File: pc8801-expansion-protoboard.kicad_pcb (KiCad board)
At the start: 2 copper layers, 219 x 95 mm, 13 parts, among them J1 Solder Side, J2 Parts Side, J3 5V, J4 12V, J5 -12V, J6 GND_1, J7 GND_2, U1 ExpansionEdge

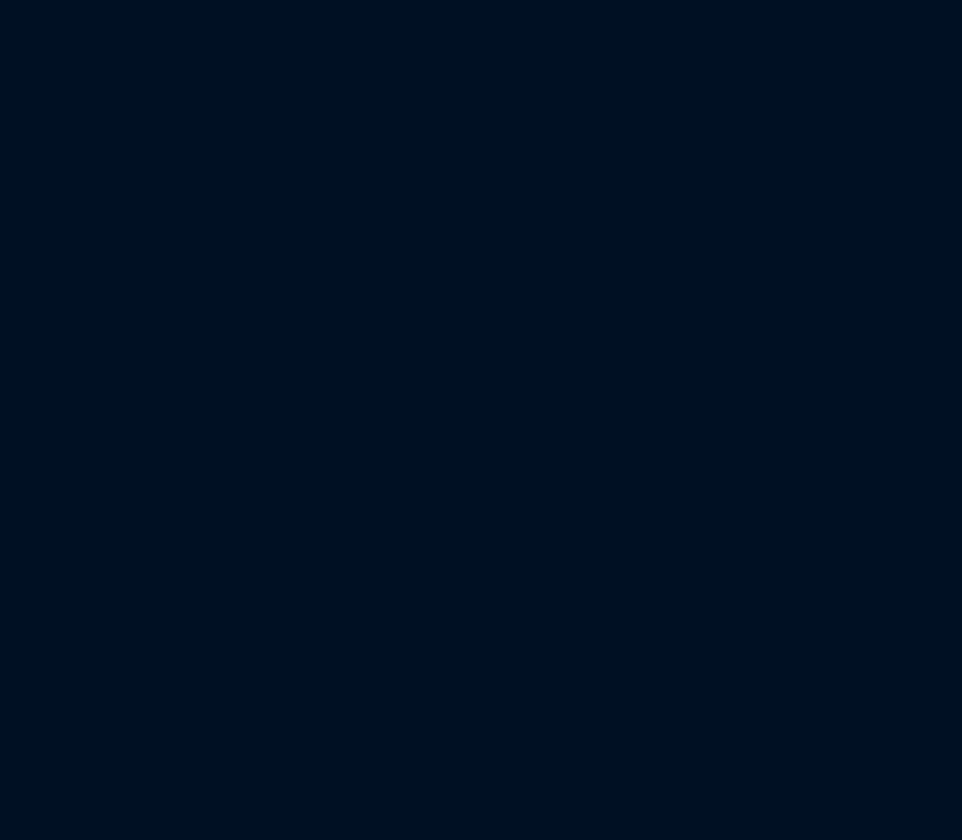
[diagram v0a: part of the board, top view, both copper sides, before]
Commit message: Flip-flops and SPI clocks added
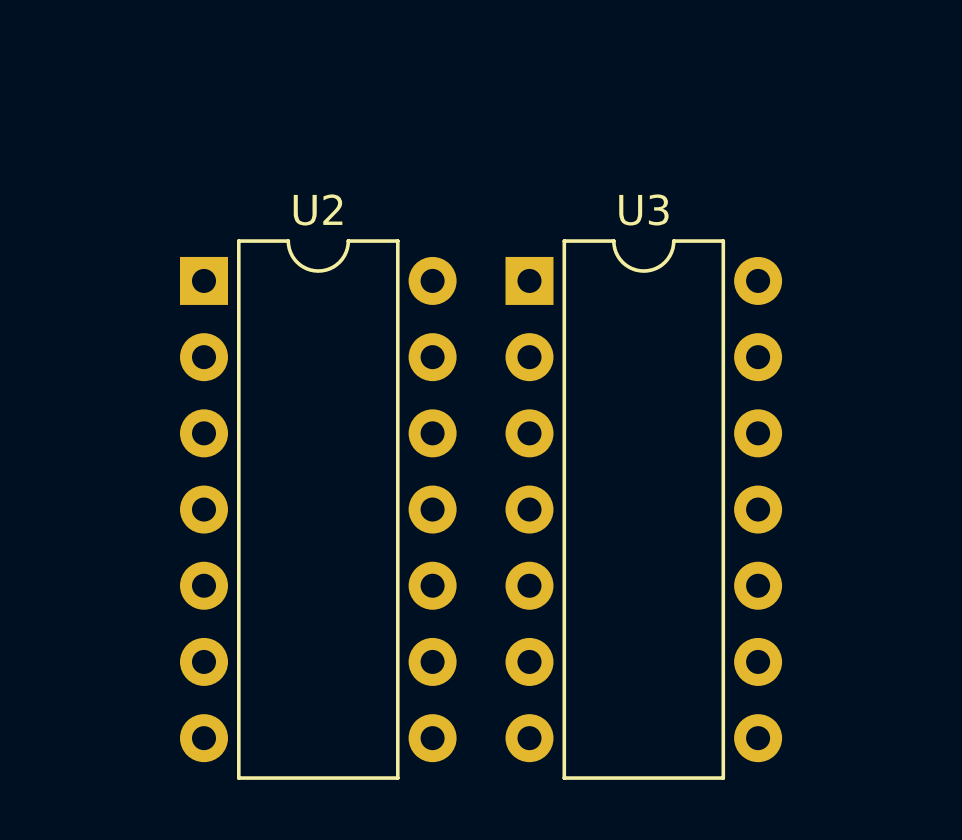
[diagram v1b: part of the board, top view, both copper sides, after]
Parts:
- added U2: 74LS32, Package_DIP:DIP-14_W7.62mm, F.Cu at (224.8, 148.8)
- added U3: 74LS04, Package_DIP:DIP-14_W7.62mm, F.Cu at (235.6, 148.8)
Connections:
- net Net-(J1-Pad10) renamed /A5
- net Net-(J1-Pad11) renamed /A6
- net Net-(J1-Pad12) renamed /A7
- net Net-(J1-Pad9) renamed /A4

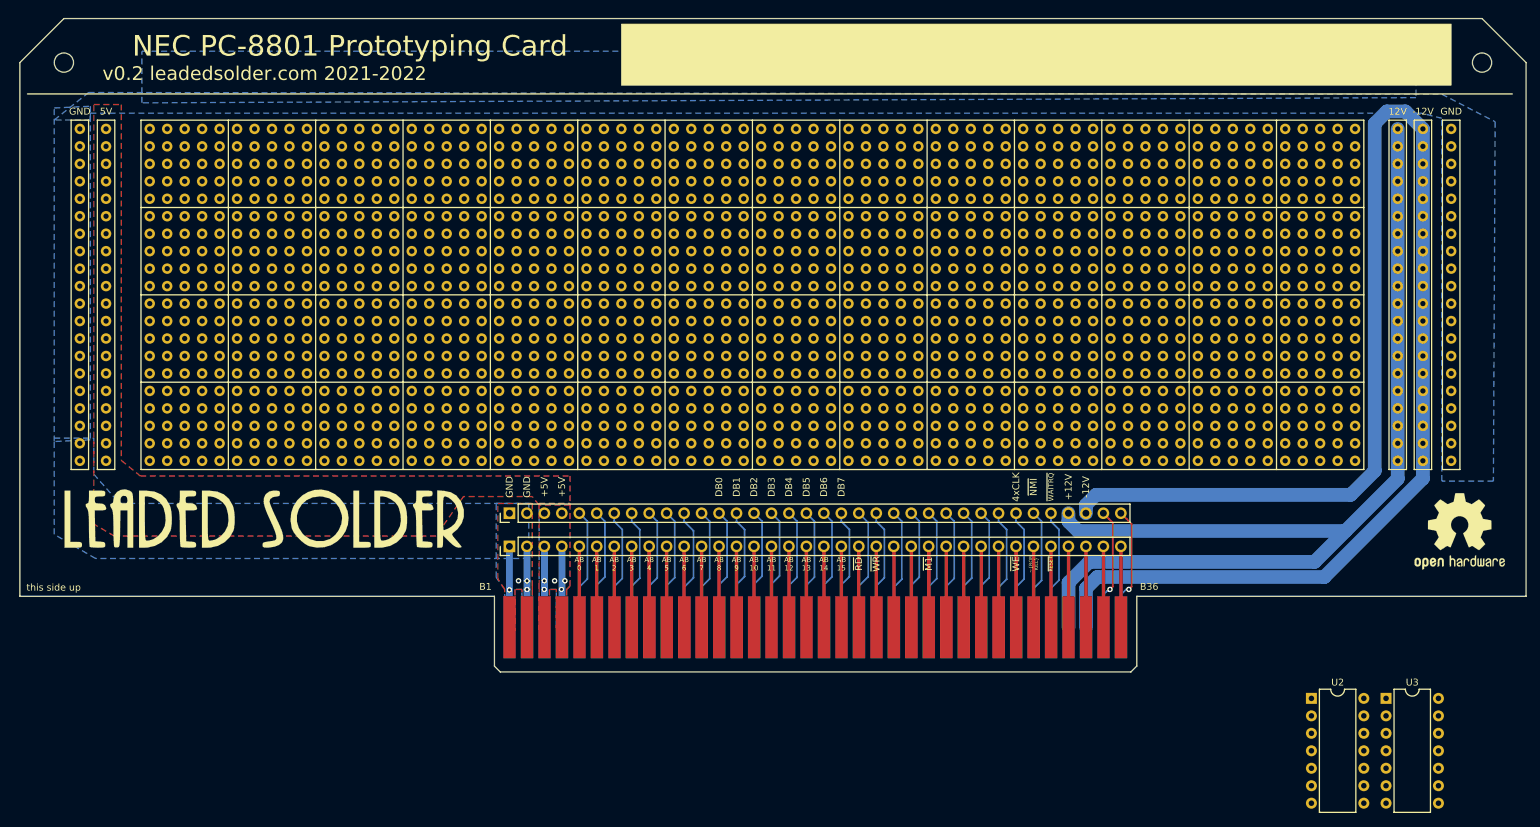
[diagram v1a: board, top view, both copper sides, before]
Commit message: Start of a DevKitC footprint
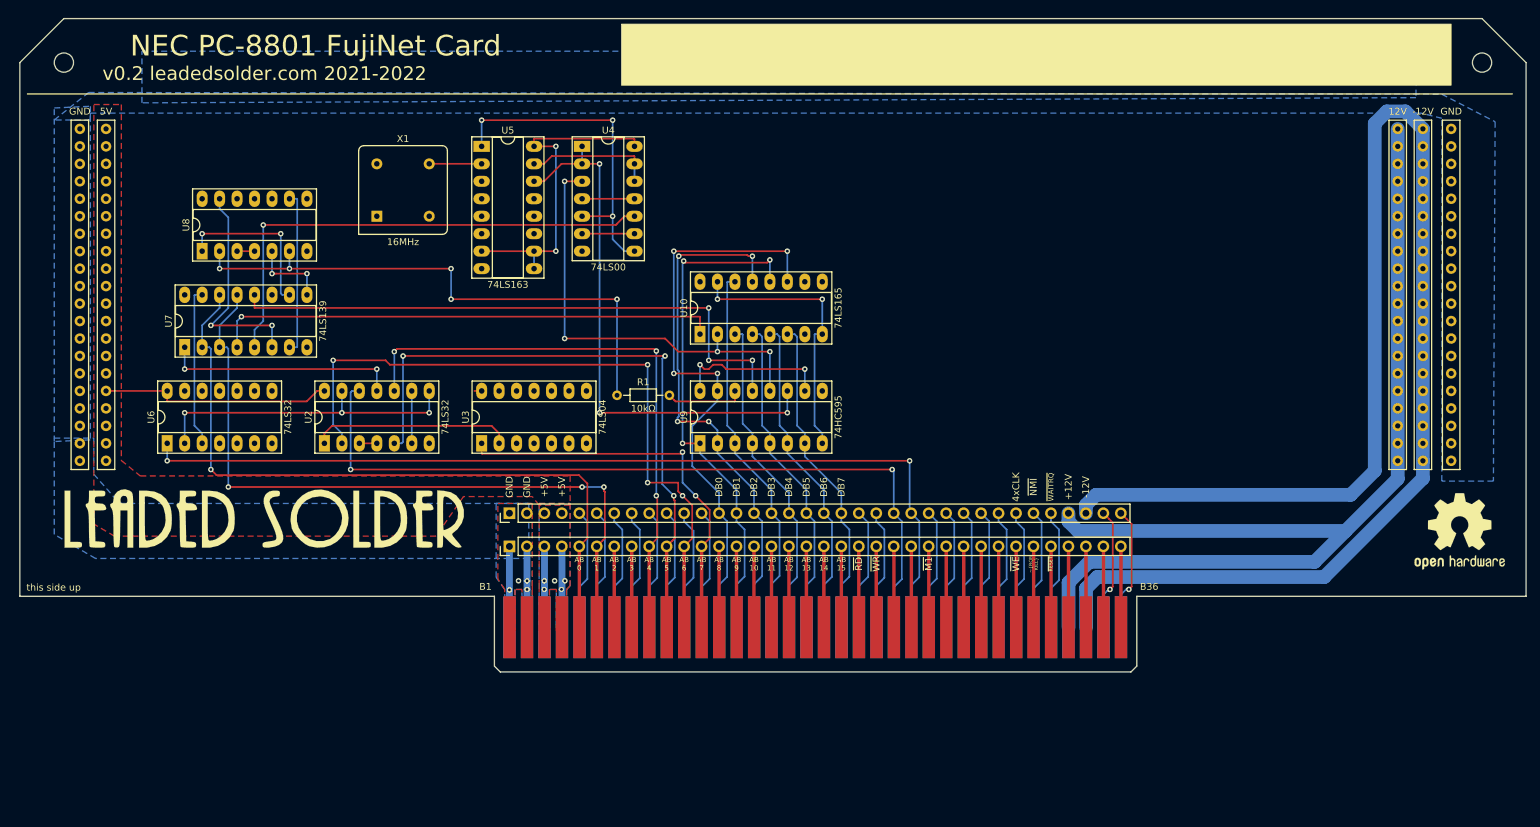
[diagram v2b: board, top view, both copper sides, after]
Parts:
- removed the REF** at (143.5, 90.2)
- added R1: 10kΩ, Resistor_THT:R_Axial_DIN0204_L3.6mm_D1.6mm_P7.62mm_Horizontal, F.Cu at (123.8, 104.8)
- added U10: 74LS165, Package_DIP:DIP-16_W7.62mm_Socket_LongPads, F.Cu at (135.9, 95.9)
- added U4: 74LS00, Package_DIP:DIP-14_W7.62mm_Socket_LongPads, F.Cu at (118.7, 68.6)
- added U5: 74LS163, Package_DIP:DIP-16_W7.62mm_Socket_LongPads, F.Cu at (104.1, 68.6)
- added U6: 74LS32, Package_DIP:DIP-14_W7.62mm_Socket_LongPads, F.Cu at (58.4, 111.8)
- added U7: 74LS139, Package_DIP:DIP-16_W7.62mm_Socket_LongPads, F.Cu at (61.0, 97.8)
- added U8: 74LS00, Package_DIP:DIP-14_W7.62mm_Socket_LongPads, F.Cu at (63.5, 83.8)
- added U9: 74HC595, Package_DIP:DIP-16_W7.62mm_Socket_LongPads, F.Cu at (135.9, 111.8)
- added X1: 16MHz, Oscillator:Oscillator_DIP-8, F.Cu at (88.9, 78.7)
- U2, U3: footprint Package_DIP:DIP-14_W7.62mm -> Package_DIP:DIP-14_W7.62mm_Socket_LongPads
- moved U2 148.2 mm to (81.3, 111.8), turned to 90 degrees
- moved U3 136.6 mm to (104.1, 111.8), turned to 90 degrees
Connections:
- net Net-(J1-Pad5) renamed /A0
- net Net-(J1-Pad6) renamed /A1
- net Net-(J1-Pad7) renamed /A2
- net Net-(J1-Pad8) renamed /A3
- net Net-(J2-Pad13) renamed /D0
- net Net-(J2-Pad14) renamed /D1
- net Net-(J2-Pad15) renamed /D2
- net Net-(J2-Pad16) renamed /D3
- net Net-(J2-Pad17) renamed /D4
- net Net-(J2-Pad18) renamed /D5
- net Net-(J2-Pad19) renamed /D6
- net Net-(J2-Pad20) renamed /D7
- net Net-(J2-Pad24) renamed /~IOR
- J2 pad 23: Net-(J2-Pad23) -> /~IOW
- U1 pad 23B: Net-(J2-Pad23) -> /~IOW
- U2 pad 11: (no net) -> /~FUJI_WR
- U2 pad 12: (no net) -> /~IOW
- U2 pad 13: (no net) -> /~FUJI_SEL
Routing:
- net /~IOR: track 17.5 -> 135.8 mm, vias 0 -> 2
- net /~IOW: track 0.00 -> 115.3 mm, vias 0 -> 2
- net /+5V: track 23.5 -> 130.0 mm, vias 5 -> 9
- net /A1: track 11.8 -> 105.7 mm, vias 0 -> 3
- net /A0: track 11.8 -> 104.6 mm, vias 0 -> 1
- net /A6: track 11.8 -> 102.5 mm, vias 0 -> 4
- net /~SER_RD: track 0.00 -> 86.4 mm, vias 0 -> 3
- net Net-(R1-Pad1): track 0.00 -> 81.3 mm, vias 0 -> 5
- net /A5: track 11.8 -> 92.8 mm, vias 0 -> 3
- net /SPI_CLK: track 0.00 -> 79.8 mm, vias 0 -> 3
- net /~SER_WR: track 0.00 -> 73.9 mm, vias 0 -> 1
- net /A4: track 11.8 -> 84.8 mm, vias 0 -> 3
- net /~START: track 0.00 -> 72.8 mm, vias 0 -> 1
- net /D0: track 17.5 -> 86.1 mm, vias 0 -> 4
- net /~SPI_CLK: track 0.00 -> 64.3 mm, vias 0 -> 4
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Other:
- board text added: "NEC PC-8801 FujiNet Card"
- board text removed: "70 wide"
- board text removed: "NEC PC-8801 Prototyping Card"
- board text removed: "nice soldering, keep it up"

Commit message: ESP32 on board
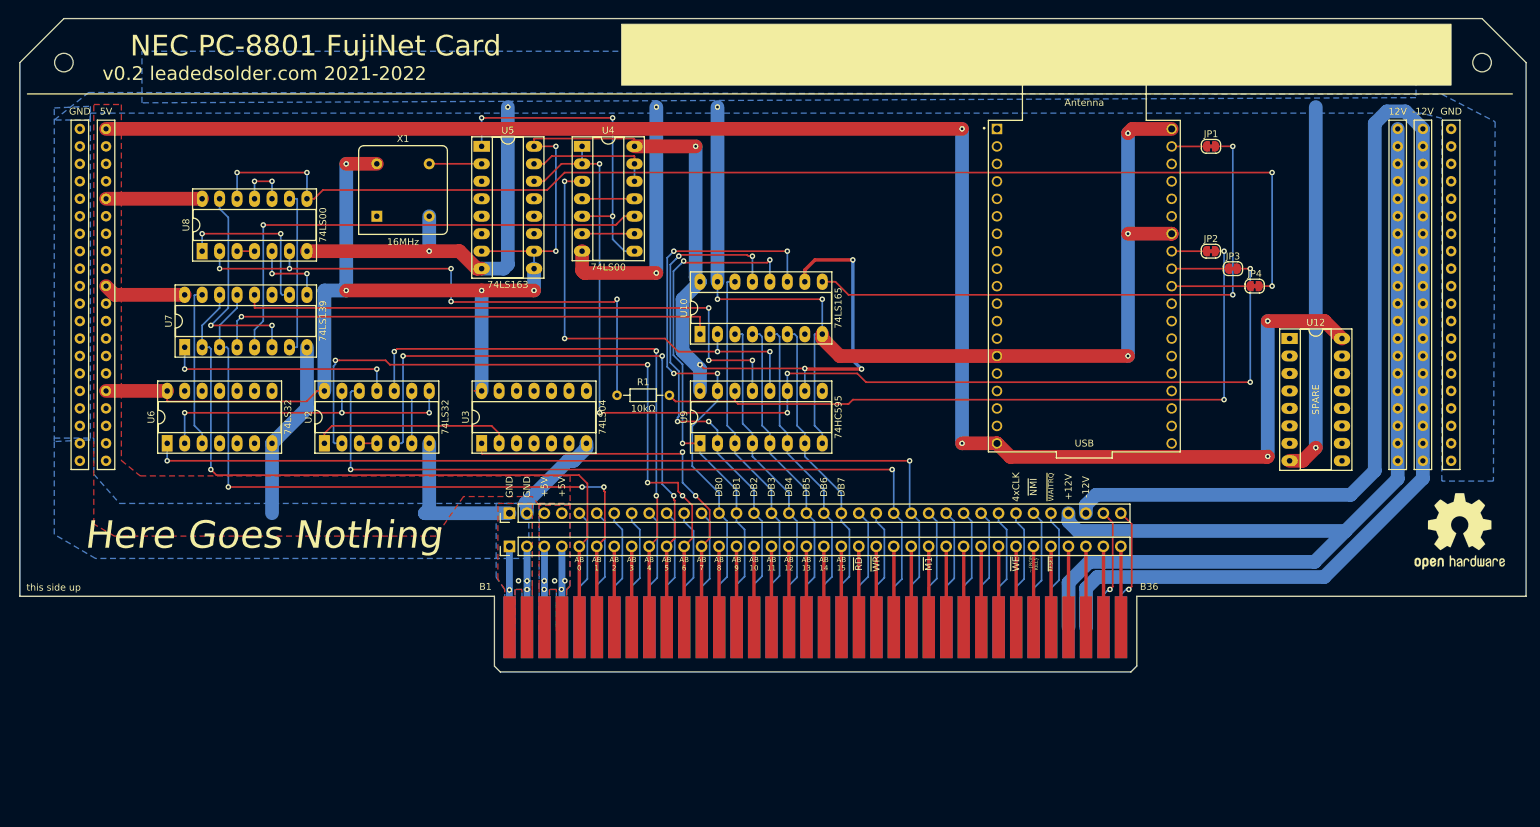
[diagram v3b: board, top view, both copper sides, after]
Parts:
- removed G***: LOGO, PC-8801:leaded-solder-logo-150dpi
- added JP1: Jumper_NC_Small, Jumper:SolderJumper-2_P1.3mm_Bridged_RoundedPad1.0x1.5mm, F.Cu at (210.2, 68.6)
- added JP2: Jumper_NC_Small, Jumper:SolderJumper-2_P1.3mm_Bridged_RoundedPad1.0x1.5mm, F.Cu at (210.2, 83.8)
- added JP3: Jumper_NC_Small, Jumper:SolderJumper-2_P1.3mm_Bridged_RoundedPad1.0x1.5mm, F.Cu at (213.4, 86.4)
- added JP4: Jumper_NC_Small, Jumper:SolderJumper-2_P1.3mm_Bridged_RoundedPad1.0x1.5mm, F.Cu at (216.5, 88.9)
- added U11: ESP32-DEVKITC, ESP32-DEVKITC:MODULE_ESP32-DEVKITC, F.Cu at (191.8, 88.9)
- added U12: 74LS139, Package_DIP:DIP-16_W7.62mm_Socket_LongPads, F.Cu at (221.6, 96.5)
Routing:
- net /+5V: track 130.0 -> 569.0 mm, vias 9 -> 20
- net /GND: track 63.8 -> 394.6 mm, vias 6 -> 15
- net /~FUJI_CS: track 0.00 -> 178.1 mm, vias 0 -> 4
- net /FUJI_OUT: track 11.4 -> 105.8 mm, vias 0 -> 2
- net /SPI_CLK: track 79.8 -> 168.6 mm, vias 3 -> 6
- net /FUJI_IN: track 0.00 -> 84.6 mm, vias 0 -> 2
- net /~VSPI_SS: track 0.00 -> 11.4 mm
- net /VSPI_SCK: track 0.00 -> 8.26 mm
- net Net-(U8-Pad10): track 0.00 -> 7.62 mm, vias 0 -> 2
- net /VSPI_MOSI: track 0.00 -> 5.07 mm
- net /VSPI_MISO: track 0.00 -> 5.05 mm
- net /D1: track 75.0 -> 76.1 mm
- net /D2: track 77.0 -> 77.8 mm
- net /D0: track 86.1 -> 86.9 mm
- net Net-(U4-Pad5): track 48.5 -> 49.2 mm
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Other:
- board text added: "CLK"
- board text added: "Here Goes Nothing"
- board text added: "IN"
- board text added: "MISO"
- board text added: "MOSI"
- board text added: "OUT"
- board text added: "SCK"
- board text added: "SPARE"
- board text added: "~CLK"
- board text added: "~CS"
- board text added: "~SLAVE_SELECT"

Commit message: TF + 3v3 LDO mounted
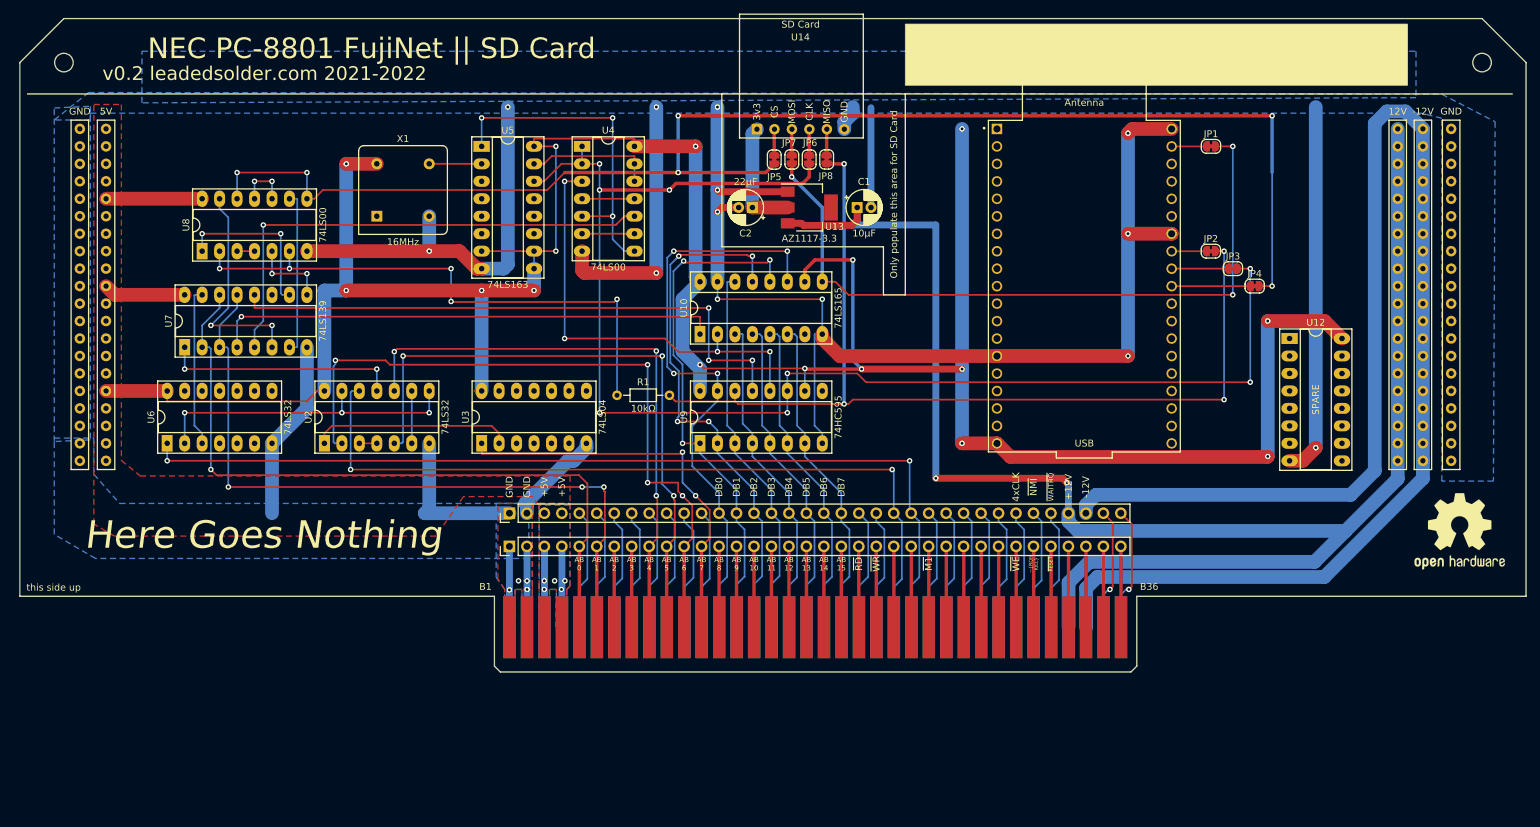
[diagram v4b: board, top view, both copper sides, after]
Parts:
- added C1: 10µF, Capacitor_THT:CP_Radial_D5.0mm_P2.00mm, F.Cu at (158.8, 77.5)
- added C2: 22µF, Capacitor_THT:CP_Radial_D5.0mm_P2.00mm, F.Cu at (143.5, 77.5)
- added JP5: Jumper_NC_Small, Jumper:SolderJumper-2_P1.3mm_Bridged_RoundedPad1.0x1.5mm, F.Cu at (146.7, 70.5)
- added JP6: Jumper_NC_Small, Jumper:SolderJumper-2_P1.3mm_Bridged_RoundedPad1.0x1.5mm, F.Cu at (151.8, 70.5)
- added JP7: Jumper_NC_Small, Jumper:SolderJumper-2_P1.3mm_Bridged_RoundedPad1.0x1.5mm, F.Cu at (149.2, 70.5)
- added JP8: Jumper_NC_Small, Jumper:SolderJumper-2_P1.3mm_Bridged_RoundedPad1.0x1.5mm, F.Cu at (154.3, 70.5)
- added U13: AZ1117-3.3, Package_TO_SOT_SMD:SOT-223, F.Cu at (151.8, 77.5)
- added U14: microSD-Breakout, microSD_Breakout:microSD_AliExpress, F.Cu at (141.6, 67.4)
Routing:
- net /+5V: track 569.0 -> 459.1 mm, vias 20 -> 21
- net /+12V: track 153.5 -> 241.5 mm, vias 0 -> 2
- net /FUJI_OUT: track 105.8 -> 143.3 mm, vias 2 -> 4
- net /SPI_CLK: track 168.6 -> 201.7 mm, vias 6 -> 8
- net /GND: track 394.6 -> 426.5 mm, vias 15 -> 17
- net /~FUJI_CS: track 178.1 -> 209.1 mm, vias 4 -> 6
- net /FUJI_IN: track 84.6 -> 103.6 mm, vias 2 -> 3
- net /+3.3V: track 0.00 -> 16.8 mm
- net /~SD_CS: track 0.00 -> 3.77 mm
- net /SD_CLK: track 0.00 -> 3.77 mm
- net /SD_MISO: track 0.00 -> 3.76 mm
- net /SD_MOSI: track 0.00 -> 3.75 mm
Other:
- board text added: "NEC PC-8801 FujiNet || SD Card"
- board text added: "Only populate this area for SD Card"
- board text removed: "NEC PC-8801 FujiNet Card"
- board text removed: "TODO: Pull these pours further away from the ejector's "rub area""
